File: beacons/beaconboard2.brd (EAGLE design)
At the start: 101.6 x 76.2 mm, 33 parts, among them IC1 7805TV, Q1 2N3904

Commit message: Added LED breakout board and e11 eagle library
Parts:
- removed LED3, LED4, LED5: (no value), SparkFun-LED:LED5MM
- removed R3: 200, SparkFun-Resistors:AXIAL-0.4
- removed R4: 120, SparkFun-Resistors:AXIAL-0.4
- removed R5: 150, SparkFun-Resistors:AXIAL-0.4
- removed U$1, U$2, U$3: DF2-L, hmcfabstudio:D2F-L
- added J2, J3, J4: 1X2-3.5MM, adafruit:1X2-3.5MM
- added PB1, PB2: D6_PUSHBUTTON, e11:D6_PUSH_BUTTON
- C1: value (none) -> 2pF
- C2, C3: value (none) -> 47uF
- C4: value (none) -> 22pF
- C5, C6: value (none) -> 0.1uF; device SparkFun-Passives:CAP-PTH-SMALL -> SparkFun-Passives:CAP-PTH-5MM
- Q2: value (none) -> 16MHz
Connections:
- removed net N$10: LED5.A, R5.P$1
- removed net N$8: LED3.A, R3.P$1
- removed net N$9: LED4.A, R4.P$1
- net BUMPER: now also PB1.3, PB1.4, PB2.3, PB2.4; no longer U$1.NO, U$2.NO, U$3.NO
- net GND: now also J3.2, PB1.1, PB1.2, PB2.1, PB2.2; no longer LED3.K, LED4.K, LED5.K, U$1.COM, U$2.COM, U$3.COM
- net N$17: now also J3.1; no longer R5.P$2
- net N$18: now also J2.1; no longer R3.P$2
- net N$4: now also J2.2; no longer R4.P$2
- net VCC: now also J4.1, J4.2
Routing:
- net GND: track 411.9 -> 339.6 mm
- net N$10: track 18.9 -> 0.00 mm
- net N$9: track 14.3 -> 0.00 mm
- net BUMPER: track 135.0 -> 147.2 mm
- net N$8: track 10.7 -> 0.00 mm
- net N$18: track 10.2 -> 0.00 mm
- net N$4: track 7.62 -> 0.00 mm
- net N$17: track 5.08 -> 0.00 mm
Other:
- board text added: "Sherman Lam"

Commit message: Added phototransistor
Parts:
- removed J2, J3, J4: 1X2-3.5MM, adafruit:1X2-3.5MM
- added R3: 330, SparkFun-Resistors:AXIAL-0.4
- added U$1: 1X5_3.5MM_TERMINAL_BLOCK, e11:1X5_3.5MM_TERMINAL_BLOCK
- added U$2: BPW77NA, e11:TO-18
- moved LED1 10.2 mm to (33.0, 52.1)
- moved LED2 9.16 mm to (33.0, 25.4)
- moved S1 1.27 mm to (77.5, 50.8)
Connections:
- new net N$9: R3.P$1, U$2.C, U$4.26
- net GND: now also U$1.5, U$2.E; no longer J3.2
- net N$17: now also U$1.4; no longer J3.1
- net N$18: now also U$1.2; no longer J2.1
- net N$4: now also U$1.3; no longer J2.2
- net VCC: now also U$1.1; no longer J4.1, J4.2
- net VDD: now also R3.P$2
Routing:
- net N$9: track 0.00 -> 49.8 mm
- net N$17: track 0.00 -> 31.6 mm
- net N$4: track 0.00 -> 29.5 mm
- net N$18: track 0.00 -> 28.5 mm
- net N$3: track 63.5 -> 50.1 mm
- net VDD: track 106.4 -> 119.1 mm
- net VCC: track 192.2 -> 204.2 mm
- net GND: track 339.6 -> 342.5 mm
- net BUMPER: track 147.2 -> 148.2 mm
- net N$11: track 21.2 -> 21.9 mm
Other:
- board text added: "Nicholas Gonzales"
- board text removed: "November 2013"

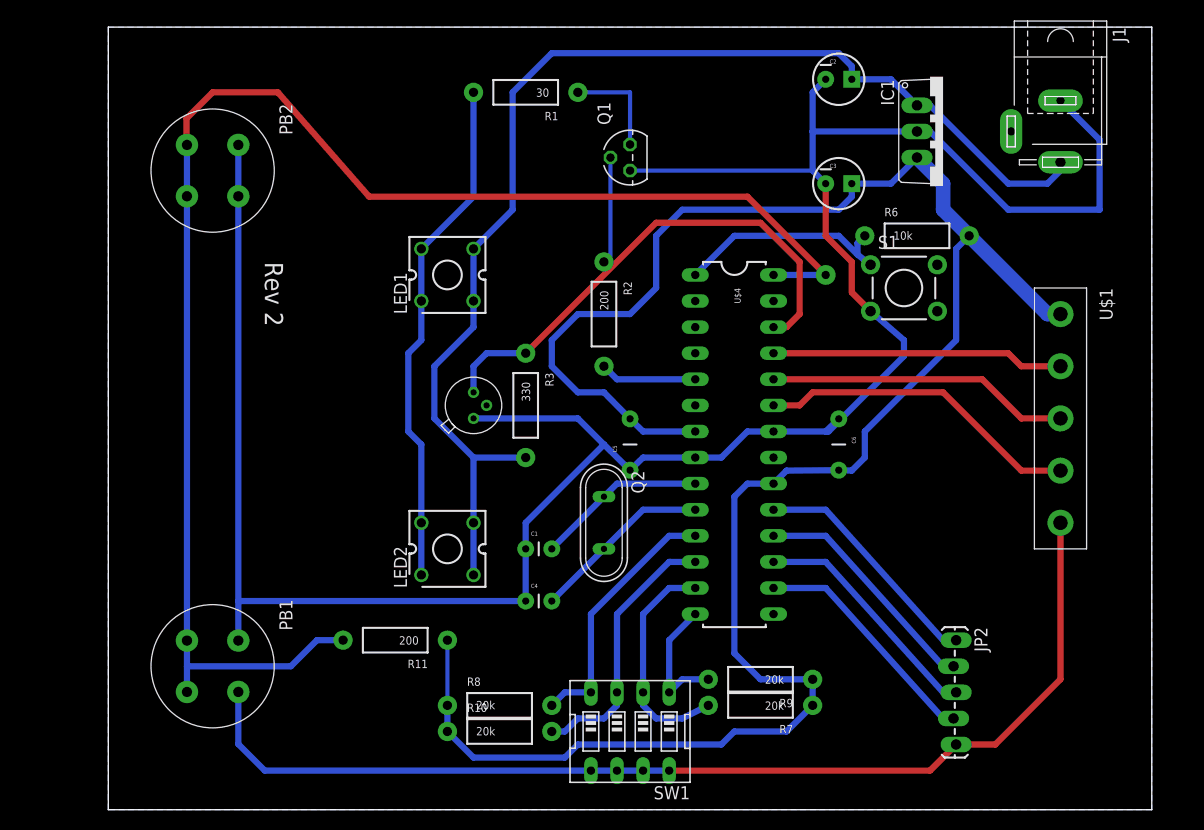
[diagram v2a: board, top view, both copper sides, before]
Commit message: Added switches for mode control
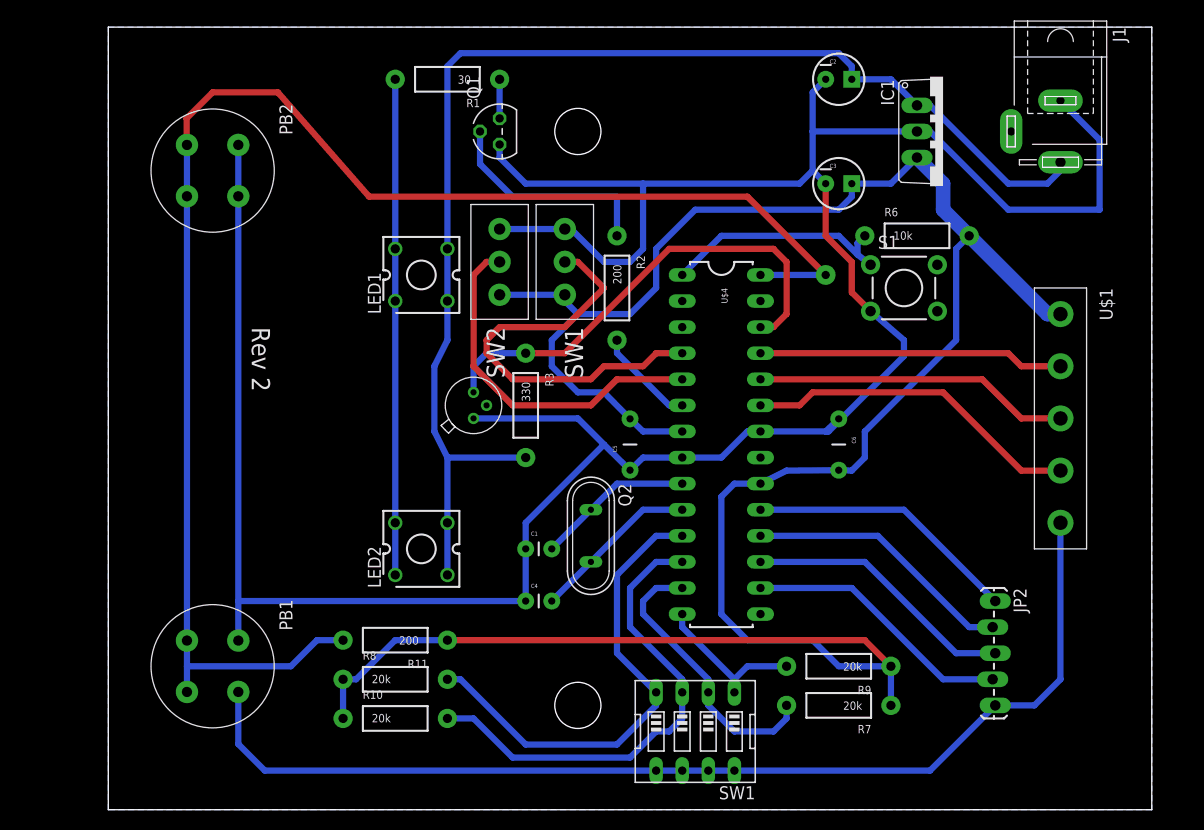
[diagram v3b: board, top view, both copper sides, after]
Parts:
- added MODE1, MODE2: SPD_SLIDE_SWITCH, e11:SPDT_SLIDE_SWITCH
- moved Q1 13.0 mm to (38.1, 66.0)
- moved R8 10.5 mm to (27.9, 12.7)
- moved R10 10.2 mm to (27.9, 8.89)
- moved R9 7.73 mm to (71.1, 14.0)
- moved R1 7.73 mm to (33.0, 71.1)
- moved R7 7.62 mm to (71.1, 10.2)
- moved SW1 6.35 mm to (57.1, 7.62)
- moved JP2 5.39 mm to (86.4, 20.3)
- moved R2 2.84 mm to (49.5, 50.8)
- moved LED1 2.54 mm to (30.5, 52.1)
- moved LED2 2.54 mm to (30.5, 25.4)
- moved Q2 1.80 mm to (47.0, 26.7)
- moved U$4 1.27 mm to (59.7, 35.6)
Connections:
- new net MODE1: MODE1.2, U$4.4
- new net MODE2: MODE2.2, U$4.5
- net GND: now also MODE1.3, MODE2.3
- net NPN_BASE: now also U$4.6; no longer U$4.5
- net VCC: now also MODE1.1, MODE2.1
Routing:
- net MODE1: track 0.00 -> 40.8 mm
- net GND: track 342.5 -> 380.2 mm
- net MODE2: track 0.00 -> 34.9 mm
- net VCC: track 204.2 -> 229.1 mm
- net N$15: track 25.3 -> 46.7 mm
- net N$16: track 26.0 -> 47.0 mm
- net N$2: track 10.8 -> 21.6 mm
- net N$1: track 10.2 -> 3.81 mm
- net VDD: track 119.1 -> 125.3 mm
- net N$14: track 22.2 -> 27.6 mm
- net N$9: track 49.8 -> 46.4 mm
- net N$5: track 23.4 -> 26.5 mm
- net N$7: track 23.4 -> 26.5 mm
- net N$6: track 23.2 -> 26.3 mm
- net N$20: track 23.2 -> 26.3 mm
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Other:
- board text added: "SW1"
- board text added: "SW2"

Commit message: Added beaconboard 3, extended version
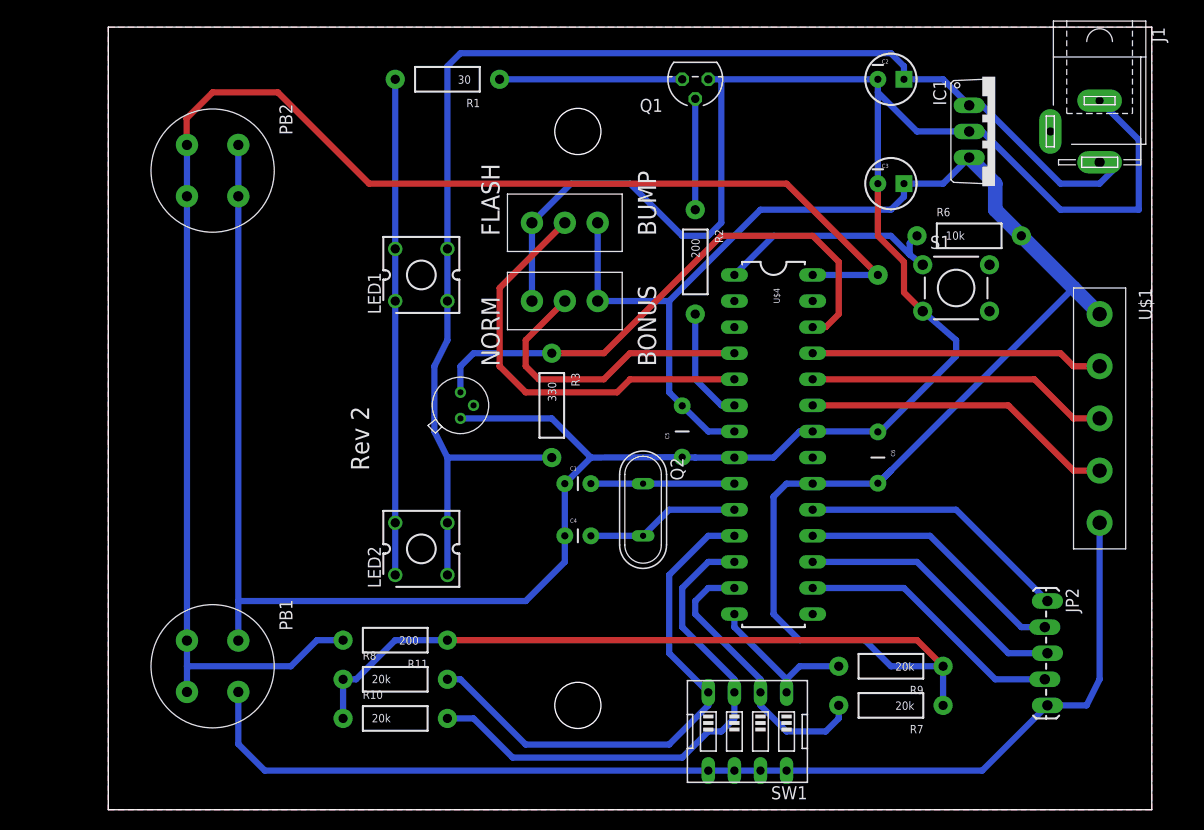
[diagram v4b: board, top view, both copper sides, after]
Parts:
- moved Q1 19.7 mm to (57.1, 71.1), turned to 180 degrees
- moved R2 8.03 mm to (57.1, 53.3)
- moved C1 7.41 mm to (44.5, 31.8)
- moved C4 7.41 mm to (44.5, 26.7)
- moved MODE2 7.41 mm to (44.5, 57.1), turned to 180 degrees
- moved Q2 5.68 mm to (52.1, 29.2)
- moved C5 5.24 mm to (55.9, 36.8)
- moved C2 5.08 mm to (76.2, 71.1)
- moved C3 5.08 mm to (76.2, 61.0)
- moved IC1 5.08 mm to (86.4, 66.0)
- moved JP2 5.08 mm to (91.4, 20.3)
- moved R6 5.08 mm to (83.8, 55.9)
- moved R7 5.08 mm to (76.2, 10.2)
- moved R9 5.08 mm to (76.2, 14.0)
- moved S1 5.08 mm to (82.5, 50.8)
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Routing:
- net N$1: track 3.81 -> 17.8 mm
- net MODE1: track 40.8 -> 29.8 mm
- net N$2: track 21.6 -> 10.8 mm
- net GND: track 380.2 -> 389.6 mm
- net VDD: track 125.3 -> 133.6 mm
- net N$9: track 46.4 -> 53.8 mm
- net MODE2: track 34.9 -> 41.0 mm
- net N$15: track 46.7 -> 51.8 mm
- net N$16: track 47.0 -> 52.0 mm
- net BUMPER: track 149.5 -> 154.2 mm
- net N$17: track 32.9 -> 30.6 mm
- net VCC: track 229.1 -> 227.5 mm
- net NPN_BASE: track 9.72 -> 11.2 mm
- net N$13: track 16.4 -> 15.0 mm
- net N$12: track 15.3 -> 14.0 mm
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- added copper zone on layer 1, net GND
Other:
- board text added: "BONUS"
- board text added: "BUMP"
- board text added: "FLASH"
- board text added: "NORM"
- board text removed: "SW1"
- board text removed: "SW2"
